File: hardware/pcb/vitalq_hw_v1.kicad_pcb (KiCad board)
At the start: 4 copper layers, 36.5 x 52.2 mm, 159 parts, among them J1 USB-C, J2 LiPo pads, J3 FSR pads, J5 ECG pads, J6 EDA pads, Q1 CSD13380F3, Q2 CSD13380F3, U1 ESP32-WROOM-32E-N8R2, U10 AS7341-DLGM, U11 TMP117AIDRVR, U12 MLX90632SLD-DCB-100-SP, U13 BME280, U14 LSM6DSV80XTR, U15 TPS61240YFFR, U16 SFH 7072, U17 MAX17048G+T10, U18 W25Q512JVEIQ, U19 TCA6408ARSVR, U2 MCP73831T-2ACI/OT, U20 TMP117AIDRVR, U3 TPS63802DLAR, U4 TPS7A2018PDBVR, U5 CP2102N-A02-GQFN28R, U6 AFE4900YZR, U7 AD5940BCBZ-RL7, U8 ADS1292RIRSMT, U9 PCA9306DCUR

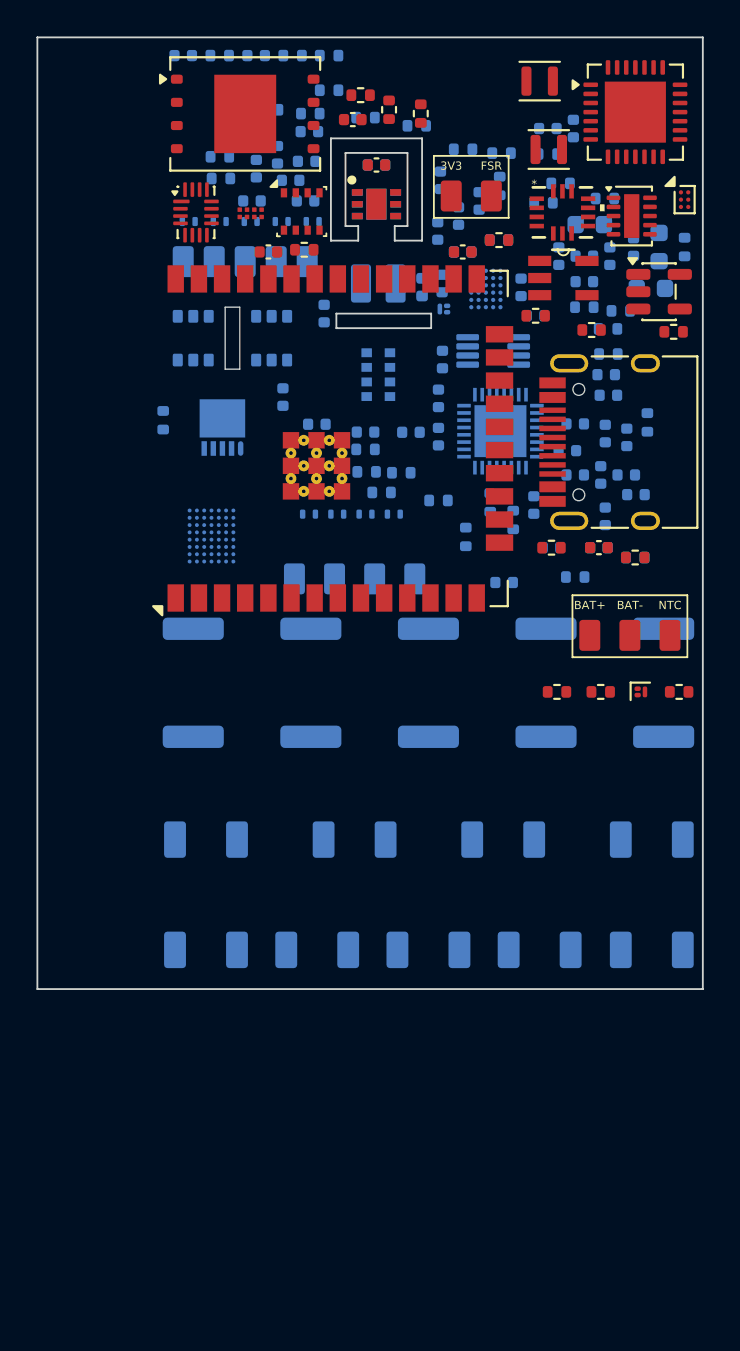
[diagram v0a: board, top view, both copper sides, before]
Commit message: Pack the protection parts onto both sides of a 36.5 by 44.4 mm board.
The pulse resistors stay on the bottom above the cluster. Both gas-discharge rows move to the top, and the cell pads sit above the resistors with the same creepage.

Co-authored-by: Riyu-D1 <Riyu-D1@users.noreply.github.com>
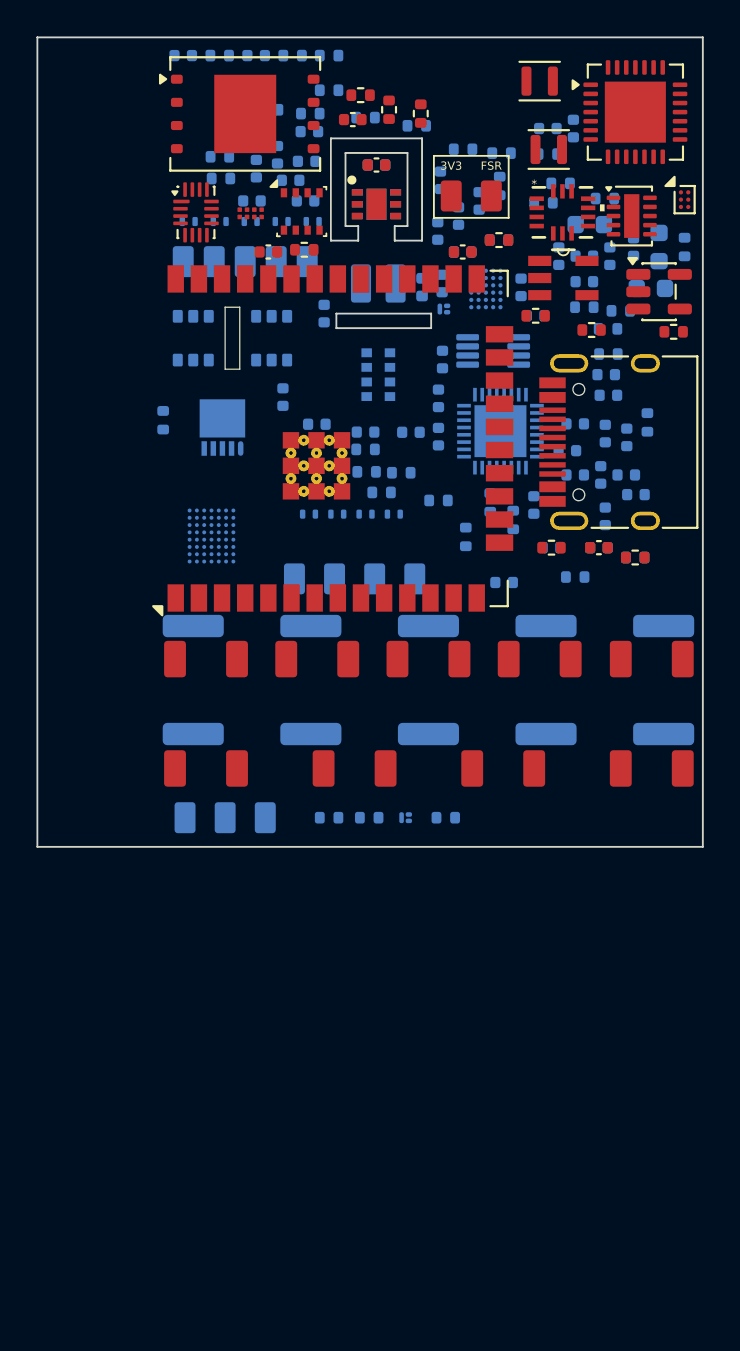
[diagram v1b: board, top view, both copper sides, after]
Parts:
- D12, D13, D14, D15, D16, D17, D18, D19, D20: moved to F.Cu
- J2, Q2, R59, R60, R61: moved to B.Cu
- moved J2 24.3 mm to (10.3, 42.8), turned to 180 degrees
- moved D12 15.9 mm to (9.25, 34.1), turned to 0 degrees
- moved D13 15.9 mm to (15.3, 34.1), turned to 0 degrees
- moved D14 15.9 mm to (21.4, 34.1), turned to 0 degrees
- moved D15 15.9 mm to (27.6, 34.1), turned to 0 degrees
- moved D16 15.9 mm to (33.7, 34.1), turned to 0 degrees
- moved Q2 14.6 mm to (20.2, 42.8), turned to 180 degrees
- moved R59 14.5 mm to (22.4, 42.8), turned to 180 degrees
- moved R60 14.5 mm to (18.2, 42.8), turned to 180 degrees
- moved R61 14.3 mm to (16.0, 42.8), turned to 180 degrees
- moved D17 3.90 mm to (9.25, 40.1), turned to 0 degrees
- moved D18 3.90 mm to (17.4, 40.1), turned to 0 degrees
- moved D19 3.90 mm to (25.6, 40.1), turned to 0 degrees
- moved D20 3.90 mm to (33.7, 40.1), turned to 0 degrees
- moved R32 0.15 mm to (8.55, 35.2)
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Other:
- board size 36.5 x 52.2 mm -> 36.5 x 44.4 mm

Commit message: Fix the CP2102N sense pin and add electrode creepage slots.
The USB sense pin was tied to 5 V. It now uses the datasheet divider, with the reset pull-up and the missing 100 nF bypasses. The TMP117 alert has its pull-up. Three slots raise creepage between the pulse resistors to 4.0 mm on a 1.6 mm board. Nothing was removed.

Co-authored-by: Riyu-D1 <Riyu-D1@users.noreply.github.com>
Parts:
- added C62: 100n, Capacitor_SMD:C_0402_1005Metric, F.Cu at (22.7, 2.55)
- added C63: 100n, Capacitor_SMD:C_0402_1005Metric, F.Cu at (25.0, 2.55)
- added R62: 1k, Resistor_SMD:R_0402_1005Metric, F.Cu at (20.4, 1.15)
- added R63: 22.1k, Resistor_SMD:R_0402_1005Metric, F.Cu at (22.7, 1.15)
- added R64: 47.5k, Resistor_SMD:R_0402_1005Metric, F.Cu at (25.0, 1.15)
- added R65: 10k, Resistor_SMD:R_0402_1005Metric, F.Cu at (20.4, 2.55)
- moved D17 0.55 mm to (9.25, 40.6)
- moved D18 0.55 mm to (17.4, 40.6)
- moved D19 0.55 mm to (25.6, 40.6)
- moved D20 0.55 mm to (33.7, 40.6)
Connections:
- U5 pad 8: VBUS -> CP_VBUS
- U5 pad 9: unconnected-(U5-~{RST}-Pad9) -> CP_RST
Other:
- outline, holes or cut-outs redrawn

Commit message: Fix the review's datasheet errors without changing respiration or the GDTs.
Replace the MCP73831 with a BQ25170 so a flat cell still charges from USB, add the missing series protection and ESP32/CP2102 passives, and withdraw the claim that respiration still works with 51 kΩ in the loop.

Co-authored-by: Riyu-D1 <Riyu-D1@users.noreply.github.com>
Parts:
- added C64: 1u, Capacitor_SMD:C_0402_1005Metric, F.Cu at (26.2, 51.0)
- added C65: 1.5n, Capacitor_SMD:C_0402_1005Metric, F.Cu at (28.4, 51.0)
- added C66: 1u, Capacitor_SMD:C_0402_1005Metric, F.Cu at (30.6, 51.0)
- added Q3: BC847BS,115, Package_TO_SOT_SMD:SOT-363_SC-70-6, F.Cu at (34.2, 51.2)
- added R66: 301k, Resistor_SMD:R_0402_1005Metric, F.Cu at (26.2, 46.6)
- added R67: 10k, Resistor_SMD:R_0402_1005Metric, F.Cu at (28.4, 46.6)
- added R68: 10k, Resistor_SMD:R_0402_1005Metric, F.Cu at (30.6, 46.6)
- added R69: 10k, Resistor_SMD:R_0402_1005Metric, F.Cu at (32.8, 46.6)
- added R70: 10k, Resistor_SMD:R_0402_1005Metric, F.Cu at (35.0, 46.6)
- added R71: 10k, Resistor_SMD:R_0402_1005Metric, F.Cu at (26.2, 48.8)
- added R72: 1k, Resistor_SMD:R_0402_1005Metric, F.Cu at (28.4, 48.8)
- added R73: 1k, Resistor_SMD:R_0402_1005Metric, F.Cu at (30.6, 48.8)
- added R74: 10k, Resistor_SMD:R_0402_1005Metric, F.Cu at (32.8, 48.8)
- added R75: 27.0k, Resistor_SMD:R_0402_1005Metric, F.Cu at (35.0, 48.8)
- added R76: 51k, Resistor_SMD:R_2512_6332Metric, B.Cu at (8.40, 49.4)
- added R77: 51k, Resistor_SMD:R_2512_6332Metric, B.Cu at (15.8, 49.4)
- added R78: 51k, Resistor_SMD:R_2512_6332Metric, B.Cu at (23.2, 49.4)
- added R79: 51k, Resistor_SMD:R_2512_6332Metric, B.Cu at (30.6, 49.4)
- R18: value 200 -> 200k
- R3: value 10k -> 3.0k
- R43, R45: value 10M -> 5.11M
- R44, R46: value 10M -> 100k
- U2: value MCP73831T-2ACI/OT -> BQ25170DSGR; footprint snap:SOT95P280X145-5N -> Package_SON:Texas_DSG0008A_WSON-8-1EP_2x2mm_P0.5mm_EP0.9x1.6mm
- moved U2 39.0 mm to (8.80, 46.6)
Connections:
- net CHG_EN renamed CHG_DIS
- C50 pad 2: IN1P -> IN1P_AC
- C51 pad 2: IN1N -> IN1N_AC
- C54 pad 1: CE_ISO -> CE_SURGE
- C54 pad 2: EDA_CE_PAD -> CE_ISO
- C55 pad 1: SE0 -> SE_ISO
- C55 pad 2: SE_ISO -> SE0
- C56 pad 1: AFE_P_AC -> AFE_P_SER
- C57 pad 1: AFE_N_AC -> AFE_N_SER
- D3 pad 1: RLDOUT -> RLD_CLAMP
- D8 pad 1: RE0 -> RE_SURGE
- D9 pad 1: DE0 -> DE_SURGE
- J2 pad 3: NTC_ADC -> TS
- Q2 pad 3: PROG_RTN -> TS
- R3 pad 1: CHG_PROG -> CHG_ISET
- R3 pad 2: PROG_RTN -> GND
- R34 pad 2: RLDOUT -> RLD_CLAMP
- R39 pad 1: CE0 -> CE_ISO
- R39 pad 2: CE_ISO -> CE0
- R40 pad 1: SE_ISO -> SE_SURGE
- R40 pad 2: EDA_SE_PAD -> SE_ISO
- R41 pad 1: RE0 -> RE_SURGE
- R41 pad 2: EDA_RE_PAD -> RE0
- R42 pad 1: DE0 -> DE_SURGE
- R42 pad 2: EDA_DE_PAD -> DE0
- R43 pad 1: +3V3 -> RLDOUT
- R44 pad 1: AFE_INP -> AFE_P_AC
- R44 pad 2: GND -> AFE_P_SER
- R45 pad 1: +3V3 -> RLDOUT
- R46 pad 1: AFE_INM -> AFE_N_AC
- R46 pad 2: GND -> AFE_N_SER
- R60 pad 2: NTC_ADC -> CHG_PG
- R61 pad 1: NTC_ADC -> TS
- U1 pad 10: unconnected-(U1-IO25-Pad10) -> GAUGE_ALRT
- U1 pad 12: unconnected-(U1-IO27-Pad12) -> CHG_PG
- U1 pad 5: NTC_ADC -> unconnected-(U1-SENSOR_VN-Pad5)
- U17 pad B4: unconnected-(U17-ALRT-PadB4) -> GAUGE_ALRT
- U19 pad 1: +3V3 -> ESP_EN
- U2 pad 1: CHG_STAT -> VBUS
- U2 pad 2: GND -> CHG_ISET
- U2 pad 3: VBAT -> TS
- U2 pad 4: VBUS -> GND
- U2 pad 5: CHG_PROG -> CHG_STAT
- U5 pad 24: unconnected-(U5-~{RTS}-Pad24) -> CP_RTS
- U5 pad 25: ESP_TX -> CP_RX
- U5 pad 26: ESP_RX -> CP_TX
- U5 pad 28: unconnected-(U5-~{DTR}-Pad28) -> CP_DTR
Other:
- board size 36.5 x 44.4 mm -> 36.5 x 53.6 mm

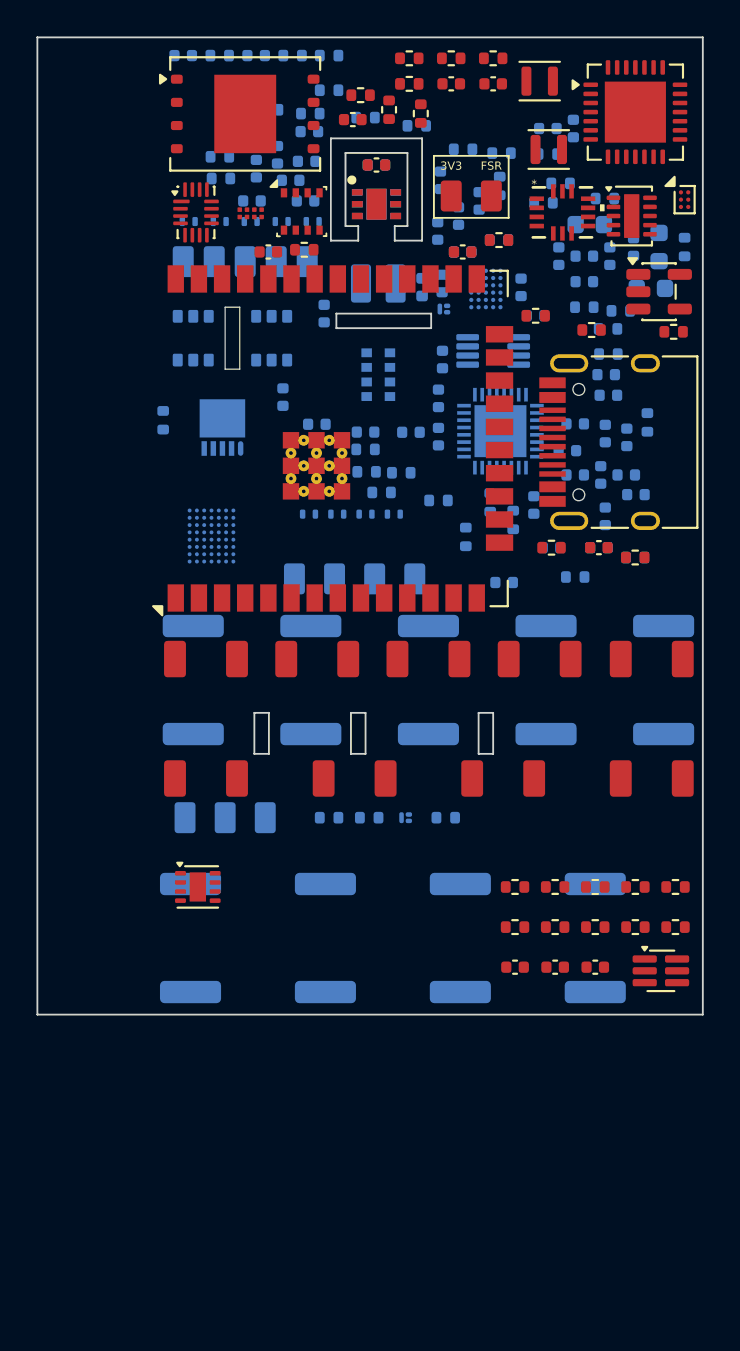
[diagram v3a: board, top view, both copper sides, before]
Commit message: Remove the gas-discharge tubes and pack the board to 36.5 by 45.6 mm.
D12-D20 and the S30 footprint are gone. Each patient line is now pad, 51 kΩ DPCR, TPD1E10B06, then the series resistor into the IC. A fourth creepage slot fills the gap the last tube was blocking.

Co-authored-by: Riyu-D1 <Riyu-D1@users.noreply.github.com>
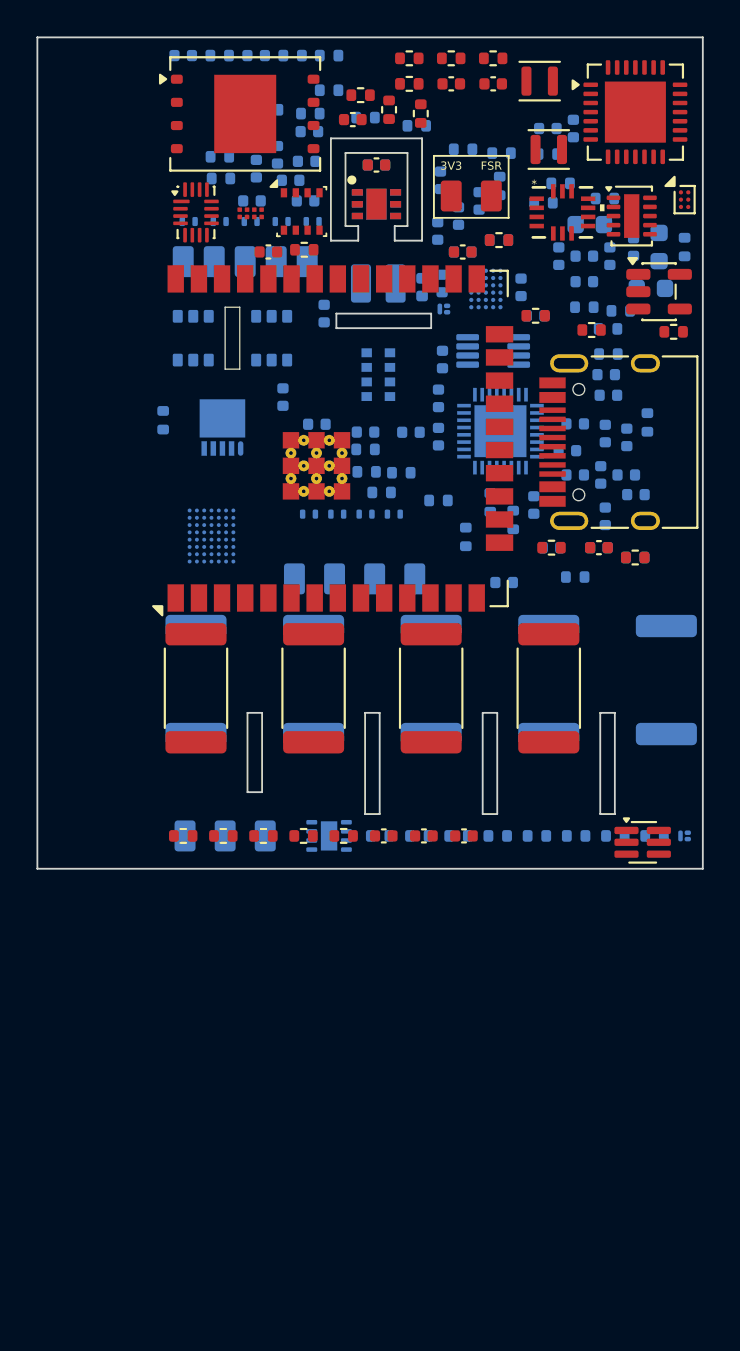
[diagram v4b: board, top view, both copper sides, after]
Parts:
- removed D12, D13, D14, D15, D16, D17, D18, D19, D20: S30-A90X, vitalq:GDT_S30
- R59, R60, R61, R76, R77, R78, R79: moved to F.Cu
- R66, R67, R68, R69, R70, R71, R72, R73, U2: moved to B.Cu
- moved R75 18.9 mm to (16.8, 43.8)
- moved R74 18.9 mm to (14.6, 43.8)
- moved Q2 15.3 mm to (35.5, 43.8)
- moved R59 14.4 mm to (8.00, 43.8), turned to 0 degrees
- moved R79 13.9 mm to (28.1, 35.7)
- moved R78 13.8 mm to (21.6, 35.7)
- moved R77 13.7 mm to (15.2, 35.7)
- moved R76 13.7 mm to (8.70, 35.7)
- moved C66 10.2 mm to (23.4, 43.8)
- moved C64 10.2 mm to (19.0, 43.8)
- moved C65 10.2 mm to (21.2, 43.8)
- moved R70 8.10 mm to (27.4, 43.8), turned to 180 degrees
- moved R60 8.06 mm to (10.2, 43.8), turned to 0 degrees
- moved R69 8.05 mm to (25.2, 43.8), turned to 180 degrees
- moved R68 8.01 mm to (23.1, 43.8), turned to 180 degrees
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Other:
- board size 36.5 x 53.6 mm -> 36.5 x 45.6 mm

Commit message: Add a 4-wire chest respiration path on the AD5940.
The ADS1292R modulation network stays. Chest breathing uses four dedicated pads into AIN1, AIN0, AIN3, and AIN2, with the same pad-side surge chain and the datasheet isolation capacitors. Shoulder EDA remains on CE0, SE0, RE0, and DE0.

Co-authored-by: Riyu-D1 <Riyu-D1@users.noreply.github.com>
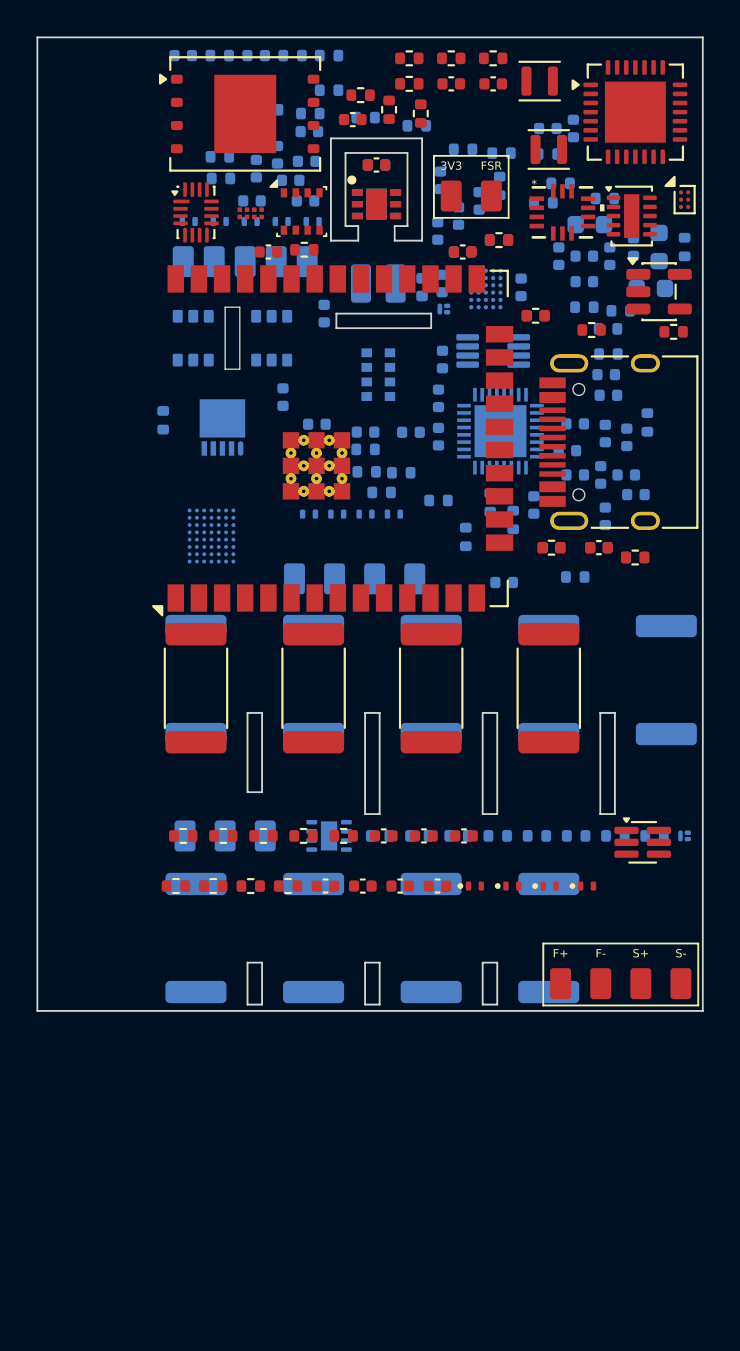
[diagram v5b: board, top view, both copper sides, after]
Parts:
- added C67: 15n, Capacitor_SMD:C_0402_1005Metric, F.Cu at (15.8, 46.5)
- added C68: 470n, Capacitor_SMD:C_0402_1005Metric, F.Cu at (17.9, 46.5)
- added C69: 470n, Capacitor_SMD:C_0402_1005Metric, F.Cu at (19.9, 46.5)
- added C70: 470n, Capacitor_SMD:C_0402_1005Metric, F.Cu at (21.9, 46.5)
- added D21: TPD1E10B06, vitalq:TPD1E10B06_DPY, F.Cu at (24.0, 46.5)
- added D22: TPD1E10B06, vitalq:TPD1E10B06_DPY, F.Cu at (26.1, 46.5)
- added D23: TPD1E10B06, vitalq:TPD1E10B06_DPY, F.Cu at (28.1, 46.5)
- added D24: TPD1E10B06, vitalq:TPD1E10B06_DPY, F.Cu at (30.1, 46.5)
- added J7: Chest bioZ, vitalq:Pads_BIOZ, F.Cu at (32.0, 51.9)
- added R80: 51k, Resistor_SMD:R_2512_6332Metric, B.Cu at (8.70, 49.4)
- added R81: 51k, Resistor_SMD:R_2512_6332Metric, B.Cu at (15.2, 49.4)
- added R82: 51k, Resistor_SMD:R_2512_6332Metric, B.Cu at (21.6, 49.4)
- added R83: 51k, Resistor_SMD:R_2512_6332Metric, B.Cu at (28.1, 49.4)
- added R84: 1k, Resistor_SMD:R_0402_1005Metric, F.Cu at (7.60, 46.5)
- added R85: 1k, Resistor_SMD:R_0402_1005Metric, F.Cu at (9.65, 46.5)
- added R86: 1k, Resistor_SMD:R_0402_1005Metric, F.Cu at (11.7, 46.5)
- added R87: 1k, Resistor_SMD:R_0402_1005Metric, F.Cu at (13.8, 46.5)
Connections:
- U7 pad A3: unconnected-(U7-AIN2-PadA3) -> BIOZ_SN
- U7 pad B3: unconnected-(U7-AIN1-PadB3) -> BIOZ_FP
- U7 pad B5: unconnected-(U7-AIN3/BUF_VREF1V8-PadB5) -> BIOZ_SP
- U7 pad D2: unconnected-(U7-AIN0-PadD2) -> BIOZ_FN
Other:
- board size 36.5 x 45.6 mm -> 36.5 x 53.4 mm
